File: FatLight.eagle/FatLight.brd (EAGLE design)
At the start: 66 x 94.9 mm, 25 parts, among them J1 12V, Q1 IRF540, Q2 IRF540, Q3 IRF540, Q4 16MHz, U1 ATMEGA328P-PU

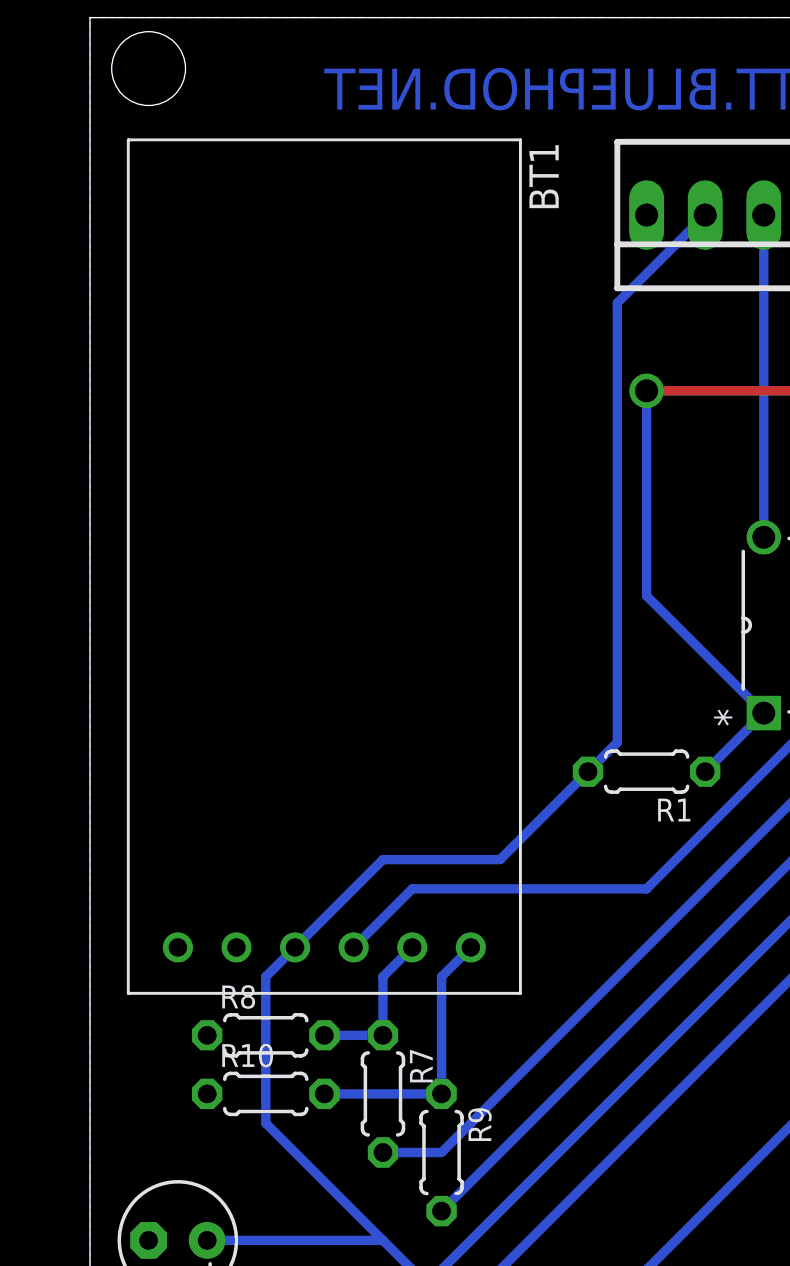
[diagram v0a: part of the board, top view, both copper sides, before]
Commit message: Bluetooth-Modul besser im Layout angeordnet.
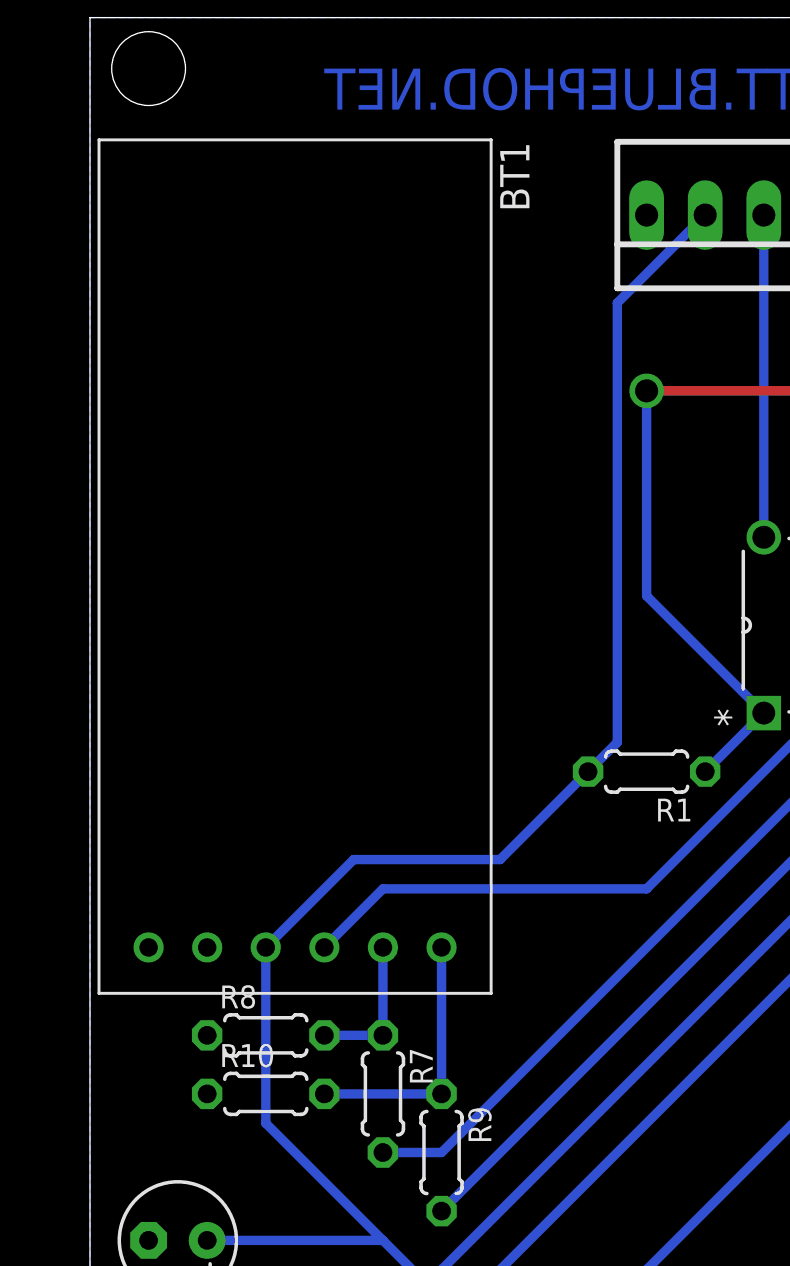
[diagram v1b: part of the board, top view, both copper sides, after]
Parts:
- moved BT1 1.27 mm to (8.89, 71.1)
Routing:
- net RXD_MCU: track 24.5 -> 25.8 mm
- net +5V: track 156.0 -> 156.7 mm
- net N$4: track 6.88 -> 6.35 mm
- net N$3: track 12.0 -> 11.4 mm
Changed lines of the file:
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@@
 </autorouter>
 <elements>
-<element name="BT1" library="ZAP-Wireless" package="HC-05-6PIN" value="BT-MODULE" x="10.16" y="71.12" rot="R270"/>
+<element name="BT1" library="ZAP-Wireless" package="HC-05-6PIN" value="BT-MODULE" x="8.89" y="71.12" rot="R270"/>
 <element name="C1" library="rcl" package="C025-025X050" value="100nF" x="43.18" y="60.96" rot="R180"/>
 <element name="C2" library="rcl" package="C025-025X050" value="100nF" x="45.72" y="76.2" rot="R180"/>
@@
 <wire x1="12.7" y1="41.91" x2="5.08" y2="41.91" width="0.4064" layer="16"/>
 <wire x1="12.7" y1="41.91" x2="7.62" y2="46.99" width="0.4064" layer="16"/>
-<wire x1="7.62" y1="46.99" x2="7.62" y2="53.34" width="0.4064" layer="16"/>
-<wire x1="7.62" y1="53.34" x2="8.89" y2="54.61" width="0.4064" layer="16"/>
+<wire x1="7.62" y1="46.99" x2="7.62" y2="54.61" width="0.4064" layer="16"/>
 <wire x1="22.86" y1="82.55" x2="26.67" y2="86.36" width="0.4064" layer="16"/>
-<wire x1="8.89" y1="54.61" x2="12.7" y2="58.42" width="0.4064" layer="16"/>
-<wire x1="12.7" y1="58.42" x2="17.78" y2="58.42" width="0.4064" layer="16"/>
+<wire x1="7.62" y1="54.61" x2="11.43" y2="58.42" width="0.4064" layer="16"/>
+<wire x1="11.43" y1="58.42" x2="17.78" y2="58.42" width="0.4064" layer="16"/>
 <wire x1="17.78" y1="58.42" x2="21.59" y2="62.23" width="0.4064" layer="16"/>
 <wire x1="54.61" y1="86.36" x2="50.8" y2="86.36" width="0.4064" layer="16"/>
@@
 <contactref element="U1" pad="2"/>
 <contactref element="BT1" pad="TXD"/>
-<wire x1="11.43" y1="54.61" x2="13.97" y2="57.15" width="0.4064" layer="16"/>
-<wire x1="13.97" y1="57.15" x2="24.13" y2="57.15" width="0.4064" layer="16"/>
+<wire x1="10.16" y1="54.61" x2="12.7" y2="57.15" width="0.4064" layer="16"/>
+<wire x1="12.7" y1="57.15" x2="24.13" y2="57.15" width="0.4064" layer="16"/>
 <wire x1="24.13" y1="57.15" x2="31.75" y2="64.77" width="0.4064" layer="16"/>
 </signal>
@@
 <contactref element="R10" pad="2"/>
 <wire x1="10.16" y1="48.26" x2="15.24" y2="48.26" width="0.4064" layer="16"/>
-<wire x1="16.51" y1="54.61" x2="15.24" y2="53.34" width="0.4064" layer="16"/>
-<wire x1="15.24" y1="53.34" x2="15.24" y2="48.26" width="0.4064" layer="16"/>
+<wire x1="15.24" y1="54.61" x2="15.24" y2="48.26" width="0.4064" layer="16"/>
 </signal>
 <signal name="N$4">
@@
 <contactref element="R7" pad="1"/>
 <wire x1="10.16" y1="50.8" x2="12.7" y2="50.8" width="0.4064" layer="16"/>
-<wire x1="13.97" y1="54.61" x2="12.7" y2="53.34" width="0.4064" layer="16"/>
-<wire x1="12.7" y1="53.34" x2="12.7" y2="50.8" width="0.4064" layer="16"/>
+<wire x1="12.7" y1="54.61" x2="12.7" y2="50.8" width="0.4064" layer="16"/>
 </signal>
 </signals>

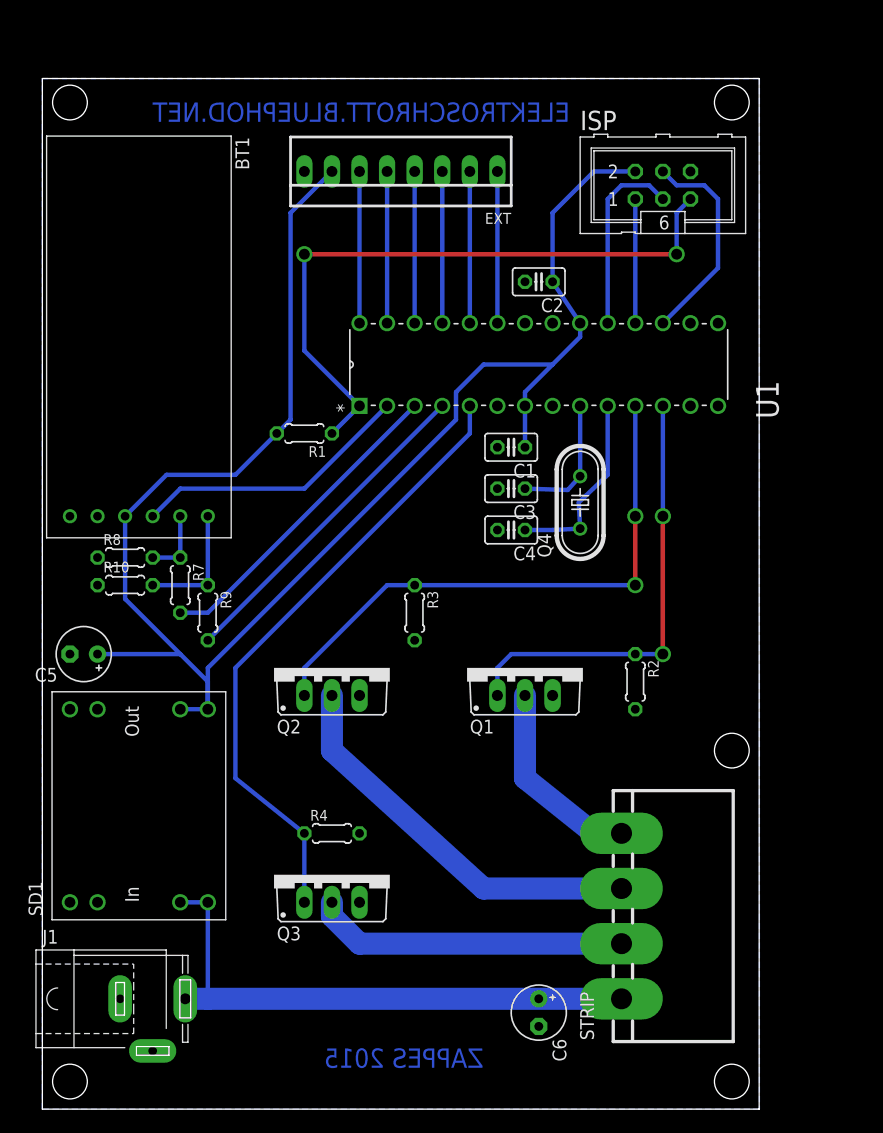
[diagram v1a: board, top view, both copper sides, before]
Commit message: Vias und Restringe vergrößert, richtige Widerstandsgrößen verwendet, Platinengröße angepasst, Kondensator für Ext-Konnektor eingefügt.
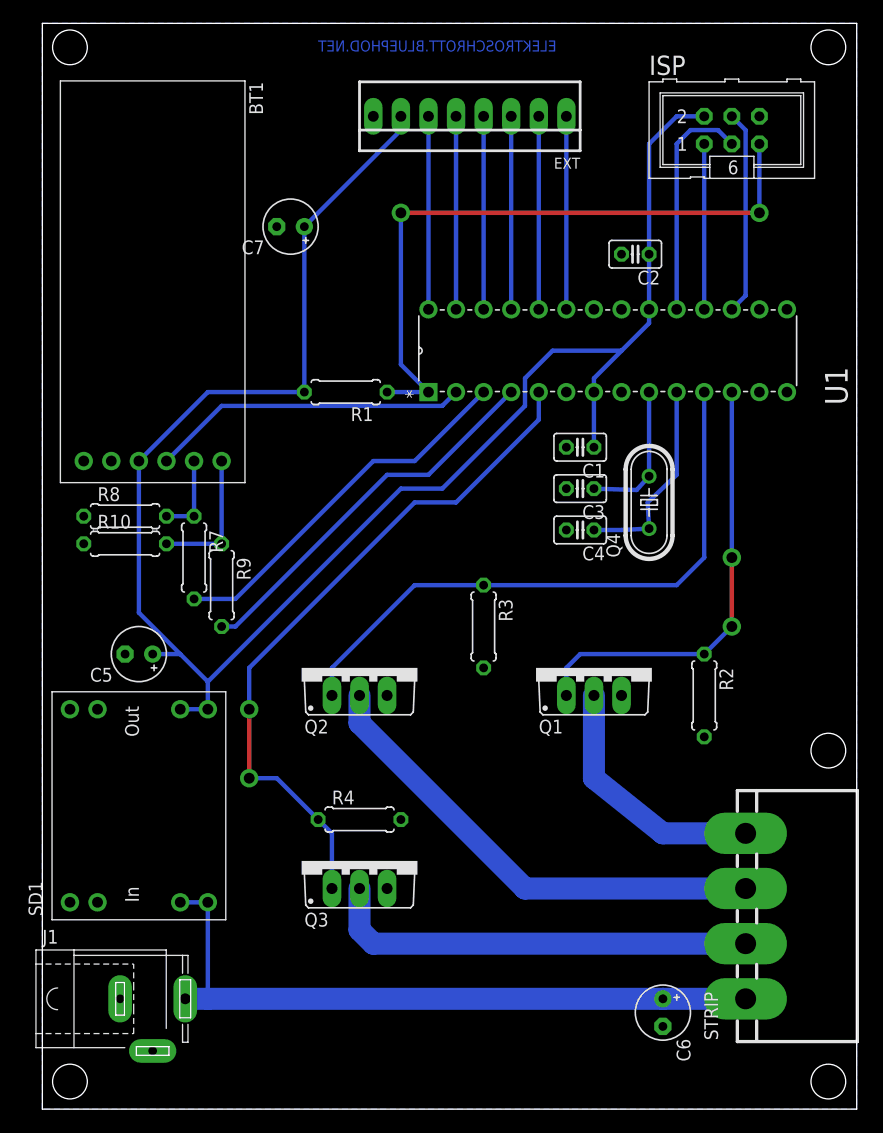
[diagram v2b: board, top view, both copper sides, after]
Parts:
- added C7: 100µF, rcl:E2,5-5
- R1, R10, R2, R3, R4, R7, R8, R9: device rcl:0204/5 -> rcl:0207/7
- moved C6 11.4 mm to (57.1, 8.89)
- moved STRIP 11.4 mm to (64.8, 17.8)
- moved C2 9.25 mm to (54.6, 78.7)
- moved ISP 8.13 mm to (63.5, 90.2)
- moved EXT 8.13 mm to (39.4, 91.4)
- moved R2 6.48 mm to (61.0, 38.1)
- moved R3 6.48 mm to (40.6, 44.5)
- moved U1 6.48 mm to (68.6, 73.7)
- moved C1 6.35 mm to (49.5, 61.0)
- moved C3 6.35 mm to (49.5, 57.1)
- moved C4 6.35 mm to (49.5, 53.3)
- moved Q4 6.35 mm to (55.9, 55.9)
- moved Q1 6.35 mm to (50.8, 40.6)
- moved R1 5.39 mm to (27.9, 66.0)
- moved BT1 5.24 mm to (10.2, 76.2)
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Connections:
- net +5V: now also C7.+
- net GND: now also C7.-
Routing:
- net +12V: track 51.6 -> 63.0 mm
- net STRIP_BLU: track 29.0 -> 39.9 mm
- net +5V: track 156.7 -> 165.9 mm
- net STRIP_GRN: track 36.7 -> 44.4 mm
- net PWM_BLU: track 57.7 -> 63.6 mm, vias 0 -> 2
- net KEY: track 30.5 -> 35.6 mm
- net TXD_MCU: track 29.5 -> 34.6 mm
- net STRIP_RED: track 18.3 -> 23.4 mm
- net MISO: track 11.4 -> 15.2 mm
- net PC5: track 14.0 -> 17.8 mm
- net PC4: track 14.0 -> 17.8 mm
- net PC3: track 14.0 -> 17.8 mm
- net PC2: track 14.0 -> 17.8 mm
- net PC1: track 14.0 -> 17.8 mm
- net PC0: track 14.0 -> 17.8 mm
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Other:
- board size 66 x 94.9 mm -> 75 x 100 mm
- board text removed: "ZAPPES 2015"

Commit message: Optimierung des Boards
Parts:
- R2, R3, R4: value 100k -> 10k
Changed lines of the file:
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@@
 <hole x="72.39" y="2.54" drill="3.2"/>
 <hole x="72.39" y="33.02" drill="3.2"/>
-<text x="25.4" y="98.425" size="1.016" layer="16" rot="MR180">ELEKTROSCHROTT.BLUEPHOD.NET</text>
+<text x="15.24" y="3.175" size="1.778" layer="16" rot="MR180">ELEKTROSCHROTT.BLUEPHOD.NET</text>
 </plain>
 <attributes>
@@
 <element name="R1" library="rcl" package="0207/7" value="10k" x="27.94" y="66.04" rot="R180"/>
 <element name="R10" library="rcl" package="0207/7" value="20k" x="7.62" y="52.07"/>
-<element name="R2" library="rcl" package="0207/7" value="100k" x="60.96" y="38.1" rot="R270"/>
-<element name="R3" library="rcl" package="0207/7" value="100k" x="40.64" y="44.45" rot="R270"/>
-<element name="R4" library="rcl" package="0207/7" value="100k" x="29.21" y="26.67"/>
+<element name="R2" library="rcl" package="0207/7" value="10k" x="60.96" y="38.1" rot="R270"/>
+<element name="R3" library="rcl" package="0207/7" value="10k" x="40.64" y="44.45" rot="R270"/>
+<element name="R4" library="rcl" package="0207/7" value="10k" x="29.21" y="26.67"/>
 <element name="R7" library="rcl" package="0207/7" value="10k" x="13.97" y="50.8" rot="R270"/>
 <element name="R8" library="rcl" package="0207/7" value="20k" x="7.62" y="54.61"/>

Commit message: Implemented Bluetooth control
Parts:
- added C8: 100nF, rcl:C025-025X050
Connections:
- new net N$5: C8.1, U1.21
- net GND: now also C8.2
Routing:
- net N$5: track 0.00 -> 12.5 mm
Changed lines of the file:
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@@
 </element>
 <element name="C7" library="rcl" package="E2,5-5" value="100µF" x="22.86" y="81.28" rot="R180"/>
+<element name="C8" library="rcl" package="C025-025X050" value="100nF" x="53.34" y="86.36" rot="R90"/>
 </elements>
 <signals>
@@
 <contactref element="U1" pad="22"/>
 <contactref element="C2" pad="2"/>
-<contactref element="C1" pad="2"/>
 <contactref element="ISP" pad="6"/>
 <contactref element="Q2" pad="S"/>
@@
 <contactref element="J1" pad="1"/>
 <contactref element="C7" pad="-"/>
+<contactref element="C1" pad="2"/>
+<contactref element="C8" pad="2"/>
 </signal>
 <signal name="+5V">
@@
 <wire x1="13.97" y1="59.69" x2="13.97" y2="54.61" width="0.4064" layer="16"/>
 </signal>
+<signal name="N$5">
+<contactref element="U1" pad="21"/>
+<contactref element="C8" pad="1"/>
+<wire x1="53.34" y1="73.66" x2="53.34" y2="74.93" width="0.4064" layer="16"/>
+<wire x1="53.34" y1="74.93" x2="54.61" y2="76.2" width="0.4064" layer="16"/>
+<wire x1="54.61" y1="76.2" x2="54.61" y2="83.82" width="0.4064" layer="16"/>
+<wire x1="54.61" y1="83.82" x2="53.34" y2="85.09" width="0.4064" layer="16"/>
+</signal>
 </signals>
